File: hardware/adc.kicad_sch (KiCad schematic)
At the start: 0 parts

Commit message: Power ve ADC sematikleri çizildi
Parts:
- added C1: 10nF, symbol Device:C
- added C2: 100nF, symbol Device:C
- added D2: SMBJ28A, Diode_THT:D_DO-35_SOD27_P7.62mm_Horizontal, symbol Diode:1N914
- added R7: 150, symbol Device:R
- added R8: 15, symbol Device:R
- added U2: AD8603, Package_TO_SOT_SMD:TSOT-23-5, symbol Amplifier_Operational:AD8603
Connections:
- new net: R7.2, R8.1
- new net +3V3: C2.1, U2.5 (V+)
- new net ADC: U2.1, U2.4 (-)
- new net GND: C1.2, C2.2, D2.2 (A), R8.2, U2.2 (V-)
- new net SENSOR: C1.1, D2.1 (K), R7.1, U2.3 (+)

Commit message: GSM module completed
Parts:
- R7: value 150 -> 150R
- R8: value 15 -> 15R
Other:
- moved on the sheet: C1, C2, D2, R7, R8, U2

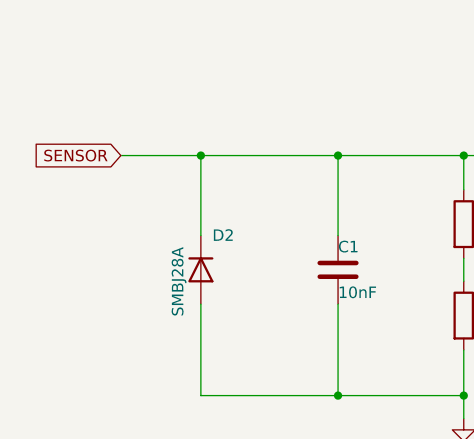
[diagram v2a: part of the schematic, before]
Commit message: * Added an EXP port (contains SPI/I2C/UART/2PINS GPIO/3V3/5V) to the MCU module * USB port connections completed * The Modules are connected to MCU module
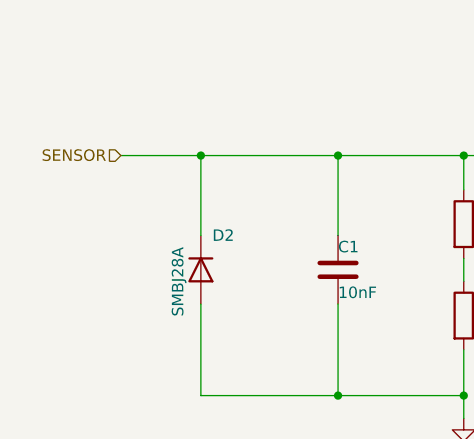
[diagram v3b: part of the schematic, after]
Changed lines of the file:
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@@
     (stroke (width 0) (type default))
   )
-  (global_label "SENSOR" (shape input) (at 99.06 78.74 180) (fields_autoplaced)
+  (hierarchical_label "SENSOR" (shape input) (at 99.06 78.74 180) (fields_autoplaced)
     (effects (font (size 1.27 1.27)) (justify right))
-    (property "Intersheetrefs" "${INTERSHEET_REFS}" (at 88.5758 78.74 0)
-      (effects (font (size 1.27 1.27)) (justify right) hide)
-    )
   )
   (hierarchical_label "ADC" (shape output) (at 170.18 81.28 0) (fields_autoplaced)
